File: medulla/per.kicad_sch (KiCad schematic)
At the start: 14 parts, among them U3 ADS1115IDGS, U4 BNO085, Y1 ABS06-32.768KHZ-1-T

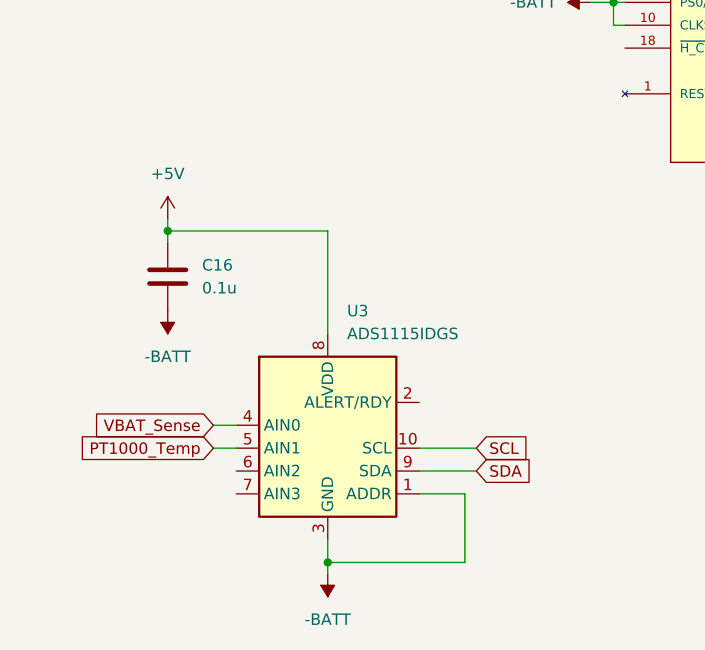
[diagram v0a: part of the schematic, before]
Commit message: alpha 0.2.0: Added RP2040, LM2936-3.3V Regulator, removed ADS1115, PCA9685
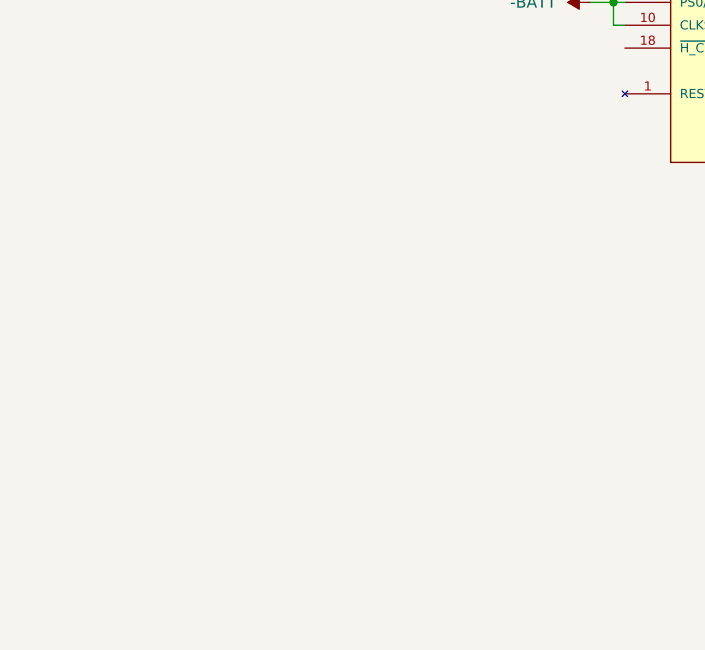
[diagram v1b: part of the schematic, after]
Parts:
- removed C16: 0.1u, symbol Device:C
- removed U3: ADS1115IDGS, Package_SO:TSSOP-10_3x3mm_P0.5mm, symbol Analog_ADC:ADS1115IDGS
